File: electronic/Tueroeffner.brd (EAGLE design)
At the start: 48.7 x 22.9 mm, 46 parts, among them IC1 IFX25001MEV33HTSA1, IC3 M25PE20, K2 EC2-12TNU, Q1 2N7002CK, Q2 2N7002CK

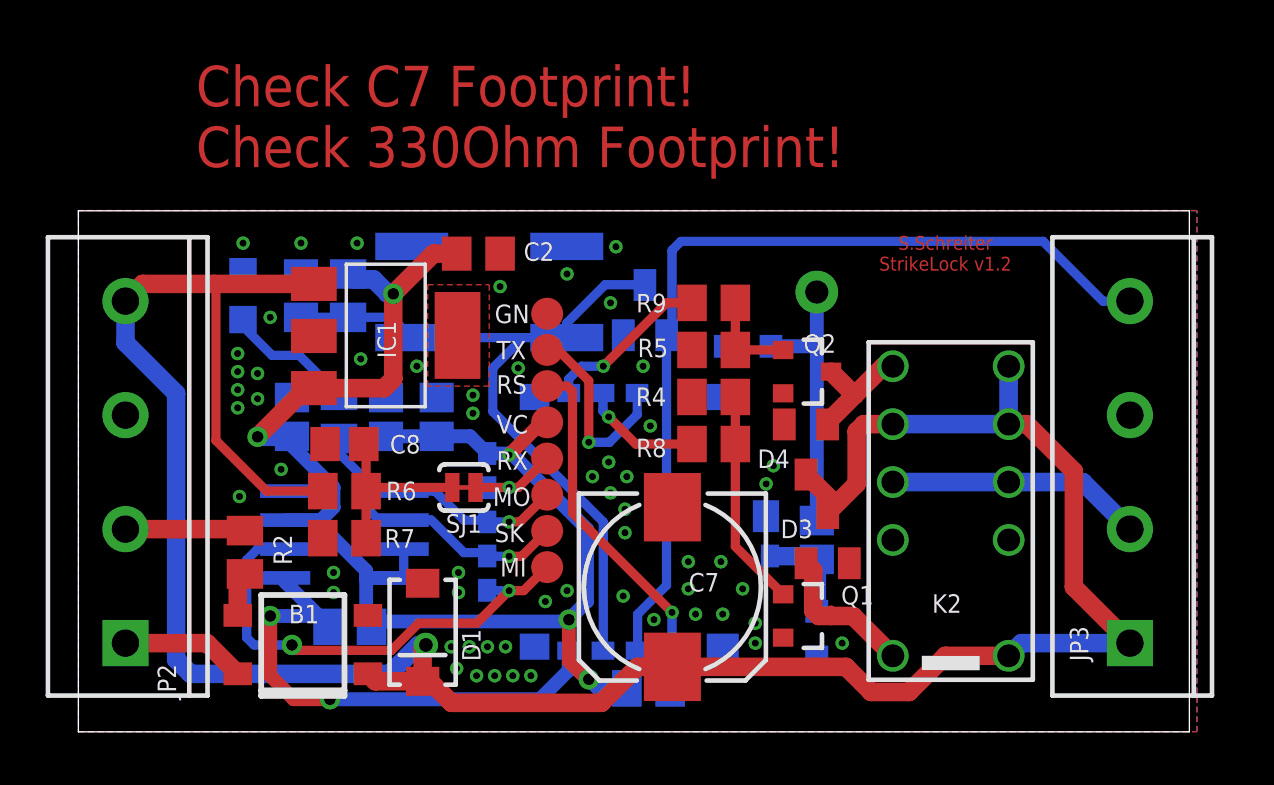
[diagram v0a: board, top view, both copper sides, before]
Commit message: Button+Led to Top
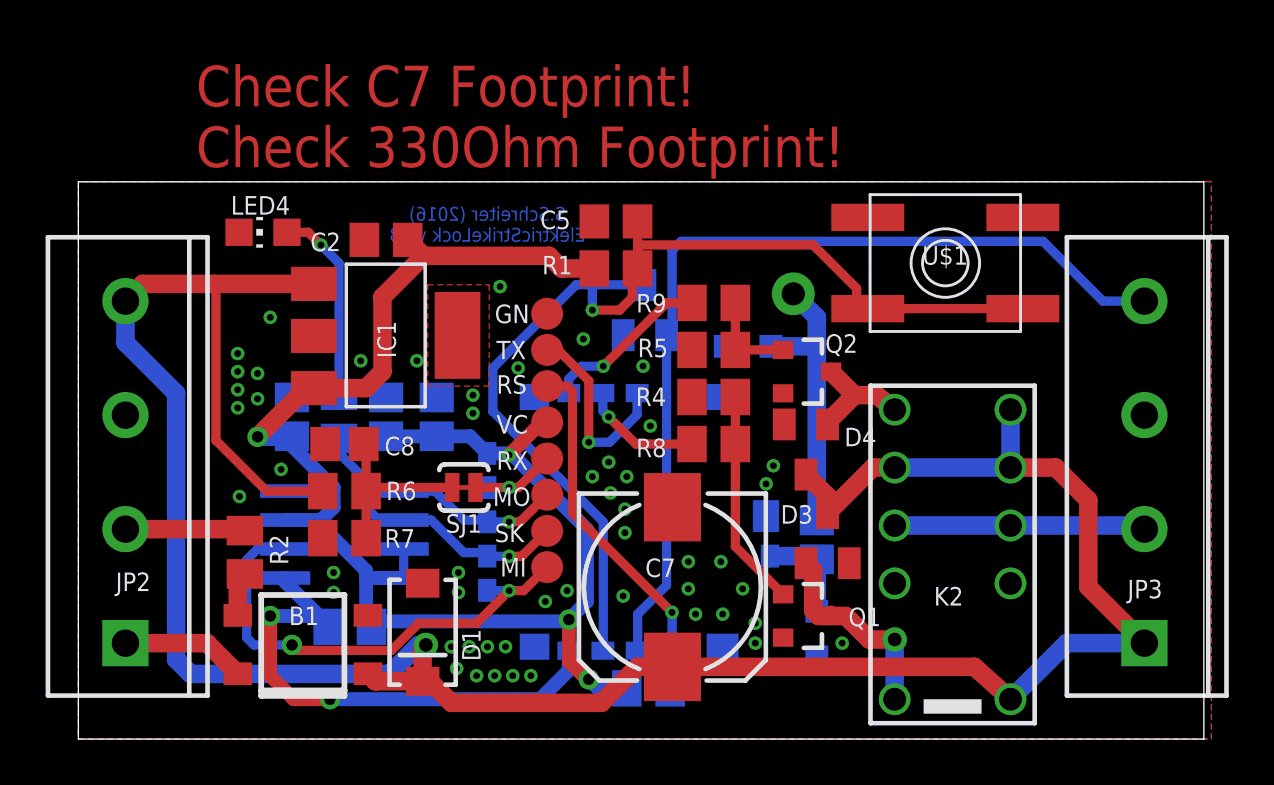
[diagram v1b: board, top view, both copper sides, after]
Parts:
- moved U$1 20.0 mm to (36.0, 19.3), flipped to the top
- moved C5 14.2 mm to (21.5, 21.1), flipped to the top, turned to 180 degrees
- moved R1 11.8 mm to (21.5, 19.1), flipped to the top, turned to 180 degrees
- moved C2 4.09 mm to (11.4, 20.3), turned to 180 degrees
- moved LED4 2.91 mm to (6.03, 20.6), flipped to the top, turned to 90 degrees
- moved K2 1.91 mm to (36.3, 6.51)
- moved JP1 1.03 mm to (29.3, 17.9)
- moved JP3 0.63 mm to (44.7, 2.62)
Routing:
- net BUTTON: track 33.1 -> 48.0 mm, vias 0 -> 1
- net VCC-3.3V: track 64.4 -> 69.0 mm, vias 5 -> 4
- net N$28: track 5.76 -> 8.64 mm, vias 0 -> 1
- net N$6: track 6.78 -> 9.19 mm, vias 0 -> 1
- net DC_5-12V: track 114.9 -> 112.7 mm
- net INT1: track 39.5 -> 40.2 mm
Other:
- board size 48.7 x 22.9 mm -> 49.4 x 24.4 mm
- board text added: "S.Schreiter (2016) ElektricStrikeLock v1.3"
- board text removed: "S.Schreiter StrikeLock v1.2"
